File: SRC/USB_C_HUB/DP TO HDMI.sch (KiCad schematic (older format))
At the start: 35 parts, among them U6 MCDP2900, U7 ZLDO1117G12TA, Y1 27MHz

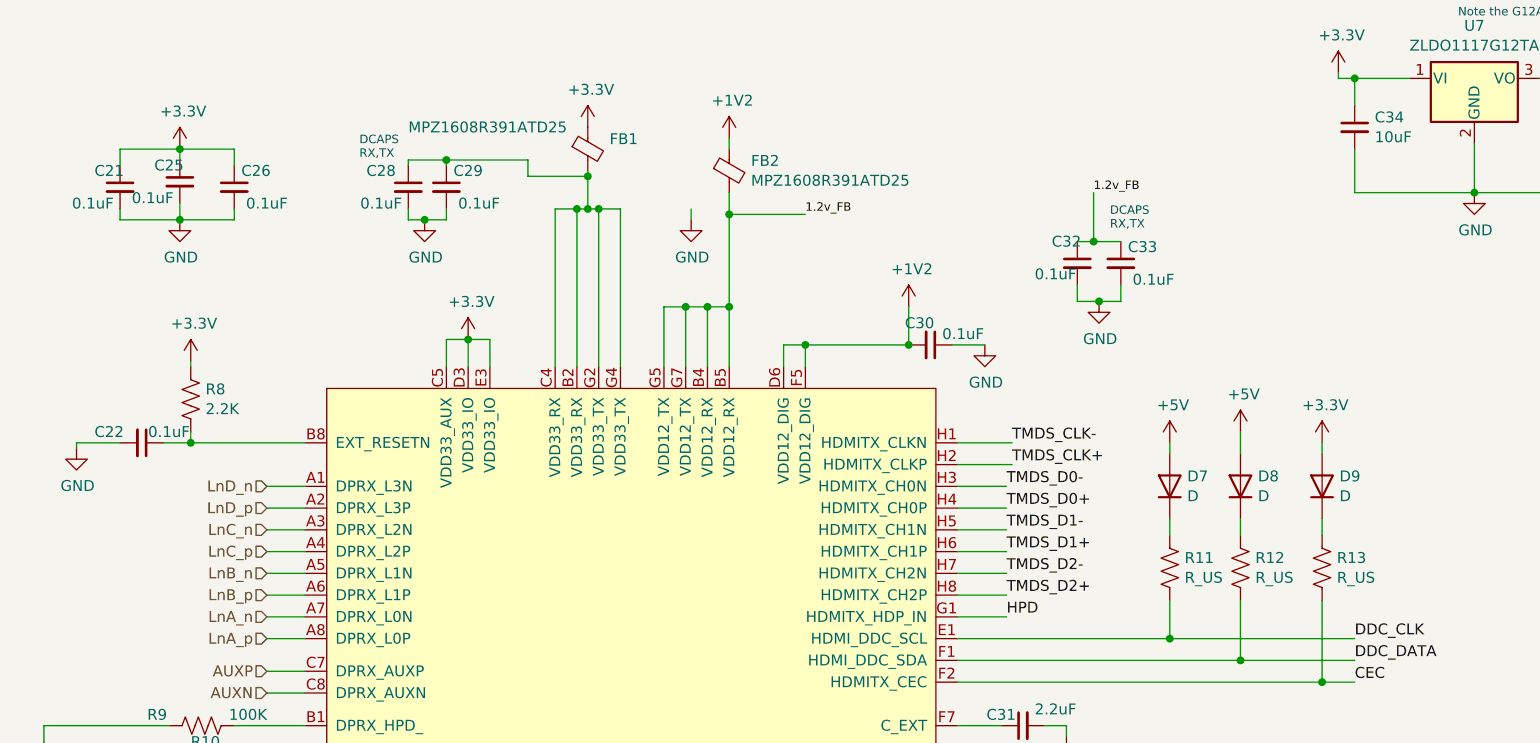
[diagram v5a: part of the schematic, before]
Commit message: schematic capture and footprint assignment complete. Pending approval
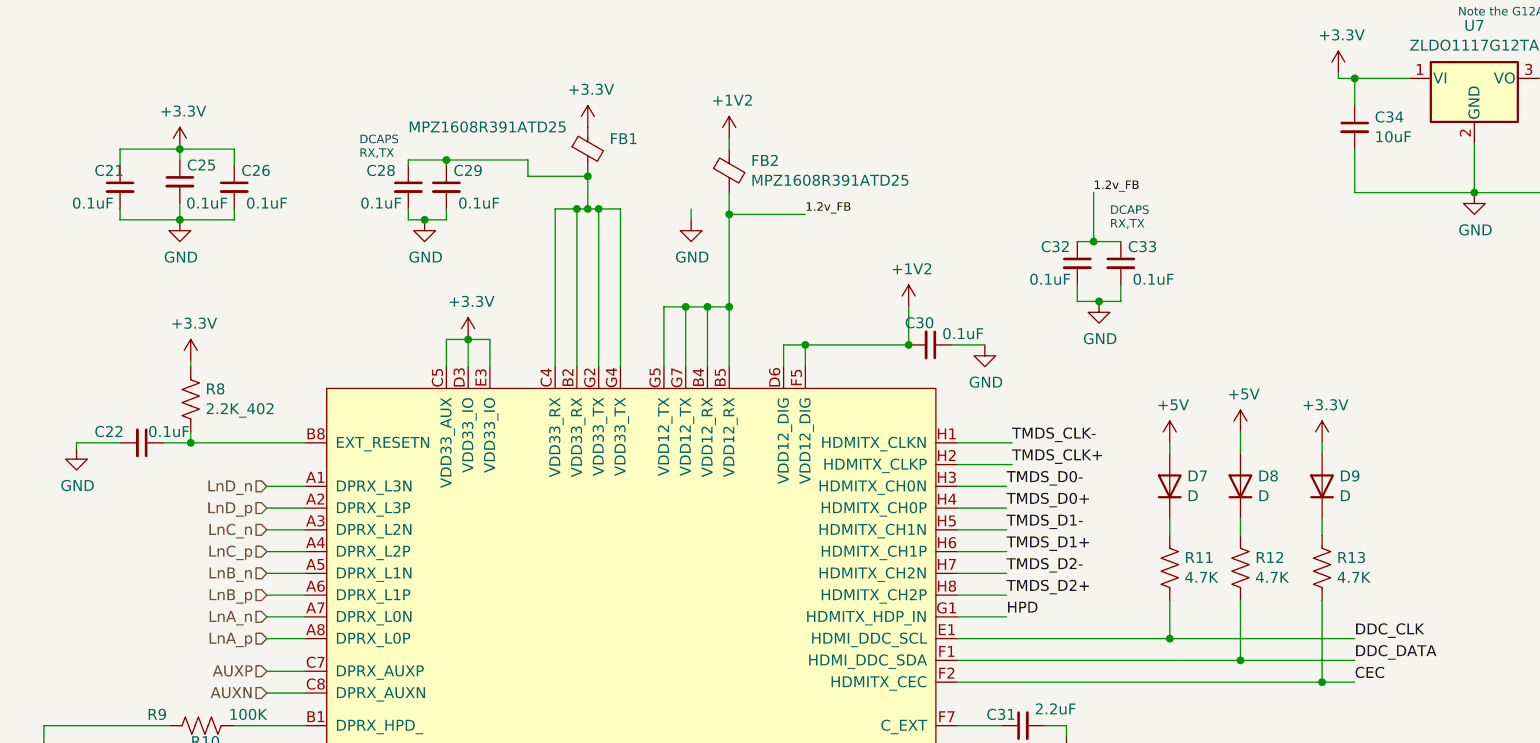
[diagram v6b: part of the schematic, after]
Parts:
- C20, C21, C22, C23, C24, C25, C26, C27, C28, C29, C30, C31, C32, C33: footprint (none) -> Capacitor_SMD:C_0402_1005Metric
- C34, C35: footprint (none) -> Capacitor_SMD:C_0603_1608Metric
- D7, D8, D9: footprint (none) -> Diode_SMD:D_SOD-323; Mfr No. (none) -> B5817WS
- FB1, FB2: footprint Resistor_SMD:R_0603_1608Metric -> Inductor_SMD:L_0603_1608Metric
- HDMI1: footprint (none) -> OLIMEX_Connectors-FP:HDMI-SWM-19
- R10: footprint (none) -> Resistor_SMD:R_0603_1608Metric; Mfr No. (none) -> ARG03BTC2490
- R11: value R_US -> 4.7K; footprint (none) -> Resistor_SMD:R_0402_1005Metric; Mfr No. (none) -> 0402WGF4701TCE
- R12, R13: value R_US -> 4.7K; footprint (none) -> Resistor_SMD:R_0402_1005Metric
- R8: value 2.2K -> 2.2K_402; footprint (none) -> Resistor_SMD:R_0402_1005Metric; Mfr No. (none) -> 0402WGJ0222TCE
- R9: footprint (none) -> Resistor_SMD:R_0805_2012Metric; Mfr No. (none) -> 0805W8F1003T5E
- U6: footprint (none) -> footprints:BGA64C100P8X8_1000X800X120N
- Y1: footprint (none) -> Crystal:Crystal_HC33-U_Horizontal_1EP_style1
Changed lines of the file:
@@
 F 0 "HDMI1" H 8431 2804 50  0000 R CNN
 F 1 "HDMI-SWM-19" H 8431 2895 50  0000 R CNN
-F 2 "" H 8605 3000 20  0001 C CNN
+F 2 "OLIMEX_Connectors-FP:HDMI-SWM-19" H 8605 3000 20  0001 C CNN
 F 3 "" H 8575 2850 60  0000 C CNN
 	1    8575 2850
@@
 P 1400 2375
 F 0 "R8" H 1468 2421 50  0000 L CNN
-F 1 "2.2K" H 1468 2330 50  0000 L CNN
-F 2 "" V 1440 2365 50  0001 C CNN
+F 1 "2.2K_402" H 1468 2330 50  0000 L CNN
+F 2 "Resistor_SMD:R_0402_1005Metric" V 1440 2365 50  0001 C CNN
 F 3 "~" H 1400 2375 50  0001 C CNN
+F 4 "0402WGJ0222TCE" H 1400 2375 50  0001 C CNN "Mfr No."
 	1    1400 2375
 	1    0    0    -1
@@
 F 0 "R10" V 1375 3975 50  0000 L CNN
 F 1 "249OHM/1%" V 1550 3800 50  0000 L CNN
-F 2 "" V 1490 4015 50  0001 C CNN
+F 2 "Resistor_SMD:R_0603_1608Metric" V 1490 4015 50  0001 C CNN
 F 3 "~" H 1450 4025 50  0001 C CNN
+F 4 "ARG03BTC2490" V 1450 4025 50  0001 C CNN "Mfr No."
 	1    1450 4025
 	0    1    1    0
@@
 F 0 "C34" H 6842 1171 50  0000 L CNN
 F 1 "10uF" H 6842 1080 50  0000 L CNN
-F 2 "" H 6750 1125 50  0001 C CNN
+F 2 "Capacitor_SMD:C_0603_1608Metric" H 6750 1125 50  0001 C CNN
 F 3 "~" H 6750 1125 50  0001 C CNN
 	1    6750 1125
@@
 F 0 "C35" H 8017 1221 50  0000 L CNN
 F 1 "10uF" H 8017 1130 50  0000 L CNN
-F 2 "" H 7925 1175 50  0001 C CNN
+F 2 "Capacitor_SMD:C_0603_1608Metric" H 7925 1175 50  0001 C CNN
 F 3 "~" H 7925 1175 50  0001 C CNN
 	1    7925 1175
@@
 F 0 "U6" H 3900 -1100 50  0000 C CNN
 F 1 "MCDP2900" H 3950 -1200 50  0000 C CNN
-F 2 "" H 5925 1475 50  0001 C CNN
+F 2 "footprints:BGA64C100P8X8_1000X800X120N" H 5925 1475 50  0001 C CNN
 F 3 "" H 5925 1475 50  0001 C CNN
 	1    3275 2325
@@
 U 1 1 61889911
 P 3225 1225
+AR Path="/64E160D5/61889911" Ref="FB1"  Part="1"
+AR Path="/6609E24E/61889911" Ref="FB1"  Part="1"
 F 0 "FB1" H 3325 1271 50  0000 L CNN
 F 1 "MPZ1608R391ATD25" H 2400 1325 50  0000 L CNN
-F 2 "Resistor_SMD:R_0603_1608Metric" V 3155 1225 50  0001 C CNN
+F 2 "Inductor_SMD:L_0603_1608Metric" V 3155 1225 50  0001 C CNN
 F 3 "~" H 3225 1225 50  0001 C CNN
 	1    3225 1225
@@
 F 0 "C29" H 2675 1475 50  0000 C CNN
 F 1 "0.1uF" H 2725 1325 50  0000 C CNN
-F 2 "" H 2575 1400 50  0001 C CNN
+F 2 "Capacitor_SMD:C_0402_1005Metric" H 2575 1400 50  0001 C CNN
 F 3 "~" H 2575 1400 50  0001 C CNN
 	1    2575 1400
@@
 F 0 "C28" H 2275 1475 50  0000 C CNN
 F 1 "0.1uF" H 2275 1325 50  0000 C CNN
-F 2 "" H 2400 1400 50  0001 C CNN
+F 2 "Capacitor_SMD:C_0402_1005Metric" H 2400 1400 50  0001 C CNN
 F 3 "~" H 2400 1400 50  0001 C CNN
 	1    2400 1400
@@
 F 0 "FB2" H 3975 1371 50  0000 L CNN
 F 1 "MPZ1608R391ATD25" H 3975 1280 50  0000 L CNN
-F 2 "Resistor_SMD:R_0603_1608Metric" V 3805 1325 50  0001 C CNN
+F 2 "Inductor_SMD:L_0603_1608Metric" V 3805 1325 50  0001 C CNN
 F 3 "~" H 3875 1325 50  0001 C CNN
 	1    3875 1325
@@
 F 0 "C20" H 950 6850 50  0000 C CNN
 F 1 "0.1uF" H 1175 6825 50  0000 C CNN
-F 2 "" H 1050 6900 50  0001 C CNN
+F 2 "Capacitor_SMD:C_0402_1005Metric" H 1050 6900 50  0001 C CNN
 F 3 "~" H 1050 6900 50  0001 C CNN
 	1    1050 6900
@@
 F 0 "Y1" V 1554 6619 50  0000 L CNN
 F 1 "27MHz" V 1645 6619 50  0000 L CNN
-F 2 "" H 1600 6375 50  0001 C CNN
+F 2 "Crystal:Crystal_HC33-U_Horizontal_1EP_style1" H 1600 6375 50  0001 C CNN
 F 3 "~" H 1600 6375 50  0001 C CNN
 F 4 "ABM8G-27.000MHZ-B4Y-T" V 1600 6375 50  0001 C CNN "Mfr No."
@@
 F 0 "C23" V 1325 6275 50  0000 C CNN
 F 1 "22pF" V 1350 6025 50  0000 C CNN
-F 2 "" H 1275 6175 50  0001 C CNN
+F 2 "Capacitor_SMD:C_0402_1005Metric" H 1275 6175 50  0001 C CNN
 F 3 "~" H 1275 6175 50  0001 C CNN
 	1    1275 6175
@@
 F 0 "C24" V 1375 6775 50  0000 C CNN
 F 1 "22pF" V 1350 6525 50  0000 C CNN
-F 2 "" H 1300 6675 50  0001 C CNN
+F 2 "Capacitor_SMD:C_0402_1005Metric" H 1300 6675 50  0001 C CNN
 F 3 "~" H 1300 6675 50  0001 C CNN
 	1    1300 6675
@@
 F 0 "C31" V 5275 3975 50  0000 C CNN
 F 1 "2.2uF" V 5300 3725 50  0000 C CNN
-F 2 "" H 5225 3875 50  0001 C CNN
+F 2 "Capacitor_SMD:C_0402_1005Metric" H 5225 3875 50  0001 C CNN
 F 3 "~" H 5225 3875 50  0001 C CNN
 	1    5225 3875
@@
 F 0 "C27" H 1600 5100 50  0000 C CNN
 F 1 "0.1uf" H 1575 5250 50  0000 C CNN
-F 2 "" H 1700 5175 50  0001 C CNN
+F 2 "Capacitor_SMD:C_0402_1005Metric" H 1700 5175 50  0001 C CNN
 F 3 "~" H 1700 5175 50  0001 C CNN
 	1    1700 5175
@@
 F 0 "C30" V 4700 2075 50  0000 C CNN
 F 1 "0.1uF" V 4750 2275 50  0000 C CNN
-F 2 "" H 4800 2125 50  0001 C CNN
+F 2 "Capacitor_SMD:C_0402_1005Metric" H 4800 2125 50  0001 C CNN
 F 3 "~" H 4800 2125 50  0001 C CNN
 	1    4800 2125
@@
 U 1 1 61AF13C1
 P 5475 1750
-F 0 "C32" H 5425 1850 50  0000 C CNN
-F 1 "0.1uF" H 5375 1700 50  0000 C CNN
-F 2 "" H 5475 1750 50  0001 C CNN
+F 0 "C32" H 5375 1825 50  0000 C CNN
+F 1 "0.1uF" H 5350 1675 50  0000 C CNN
+F 2 "Capacitor_SMD:C_0402_1005Metric" H 5475 1750 50  0001 C CNN
 F 3 "~" H 5475 1750 50  0001 C CNN
 	1    5475 1750
@@
 F 0 "C33" H 5775 1825 50  0000 C CNN
 F 1 "0.1uF" H 5825 1675 50  0000 C CNN
-F 2 "" H 5675 1750 50  0001 C CNN
+F 2 "Capacitor_SMD:C_0402_1005Metric" H 5675 1750 50  0001 C CNN
 F 3 "~" H 5675 1750 50  0001 C CNN
 	1    5675 1750
@@
 F 0 "C26" H 1700 1475 50  0000 C CNN
 F 1 "0.1uF" H 1750 1325 50  0000 C CNN
-F 2 "" H 1600 1400 50  0001 C CNN
+F 2 "Capacitor_SMD:C_0402_1005Metric" H 1600 1400 50  0001 C CNN
 F 3 "~" H 1600 1400 50  0001 C CNN
 	1    1600 1400
@@
 U 1 1 61B8F7AE
 P 1350 1375
-F 0 "C25" H 1300 1450 50  0000 C CNN
-F 1 "0.1uF" H 1225 1300 50  0000 C CNN
-F 2 "" H 1350 1375 50  0001 C CNN
+F 0 "C25" H 1450 1450 50  0000 C CNN
+F 1 "0.1uF" H 1475 1275 50  0000 C CNN
+F 2 "Capacitor_SMD:C_0402_1005Metric" H 1350 1375 50  0001 C CNN
 F 3 "~" H 1350 1375 50  0001 C CNN
 	1    1350 1375
@@
 F 0 "C21" H 1025 1475 50  0000 C CNN
 F 1 "0.1uF" H 950 1325 50  0000 C CNN
-F 2 "" H 1075 1400 50  0001 C CNN
+F 2 "Capacitor_SMD:C_0402_1005Metric" H 1075 1400 50  0001 C CNN
 F 3 "~" H 1075 1400 50  0001 C CNN
 	1    1075 1400
@@
 P 5900 3150
 F 0 "R11" H 5968 3196 50  0000 L CNN
-F 1 "R_US" H 5968 3105 50  0000 L CNN
-F 2 "" V 5940 3140 50  0001 C CNN
+F 1 "4.7K" H 5968 3105 50  0000 L CNN
+F 2 "Resistor_SMD:R_0402_1005Metric" V 5940 3140 50  0001 C CNN
 F 3 "~" H 5900 3150 50  0001 C CNN
+F 4 "0402WGF4701TCE" H 5900 3150 50  0001 C CNN "Mfr No."
 	1    5900 3150
 	1    0    0    -1
@@
 F 0 "D7" V 5946 2695 50  0000 R CNN
 F 1 "D" V 5855 2695 50  0000 R CNN
-F 2 "" H 5900 2775 50  0001 C CNN
+F 2 "Diode_SMD:D_SOD-323" H 5900 2775 50  0001 C CNN
 F 3 "~" H 5900 2775 50  0001 C CNN
+F 4 "B5817WS" V 5900 2775 50  0001 C CNN "Mfr No."
 	1    5900 2775
 	0    -1   -1   0
@@
 P 6225 3150
 F 0 "R12" H 6293 3196 50  0000 L CNN
-F 1 "R_US" H 6293 3105 50  0000 L CNN
-F 2 "" V 6265 3140 50  0001 C CNN
+F 1 "4.7K" H 6293 3105 50  0000 L CNN
+F 2 "Resistor_SMD:R_0402_1005Metric" V 6265 3140 50  0001 C CNN
 F 3 "~" H 6225 3150 50  0001 C CNN
 	1    6225 3150
@@
 F 0 "D8" V 6271 2695 50  0000 R CNN
 F 1 "D" V 6180 2695 50  0000 R CNN
-F 2 "" H 6225 2775 50  0001 C CNN
+F 2 "Diode_SMD:D_SOD-323" H 6225 2775 50  0001 C CNN
 F 3 "~" H 6225 2775 50  0001 C CNN
+F 4 "B5817WS" V 6225 2775 50  0001 C CNN "Mfr No."
 	1    6225 2775
 	0    -1   -1   0
@@
 P 6600 3150
 F 0 "R13" H 6668 3196 50  0000 L CNN
-F 1 "R_US" H 6668 3105 50  0000 L CNN
-F 2 "" V 6640 3140 50  0001 C CNN
+F 1 "4.7K" H 6668 3105 50  0000 L CNN
+F 2 "Resistor_SMD:R_0402_1005Metric" V 6640 3140 50  0001 C CNN
 F 3 "~" H 6600 3150 50  0001 C CNN
 	1    6600 3150
@@
 F 0 "D9" V 6646 2695 50  0000 R CNN
 F 1 "D" V 6555 2695 50  0000 R CNN
-F 2 "" H 6600 2775 50  0001 C CNN
+F 2 "Diode_SMD:D_SOD-323" H 6600 2775 50  0001 C CNN
 F 3 "~" H 6600 2775 50  0001 C CNN
+F 4 "B5817WS" V 6600 2775 50  0001 C CNN "Mfr No."
 	1    6600 2775
 	0    -1   -1   0
@@
 F 0 "R9" V 1400 3625 50  0000 L CNN
 F 1 "100K" V 1400 4000 50  0000 L CNN
-F 2 "" V 1490 3865 50  0001 C CNN
+F 2 "Resistor_SMD:R_0805_2012Metric" V 1490 3865 50  0001 C CNN
 F 3 "~" H 1450 3875 50  0001 C CNN
+F 4 "0805W8F1003T5E" V 1450 3875 50  0001 C CNN "Mfr No."
 	1    1450 3875
 	0    1    1    0
@@
 F 0 "C22" V 1125 2425 50  0000 C CNN
 F 1 "0.1uF" V 1125 2700 50  0000 C CNN
-F 2 "" H 1175 2575 50  0001 C CNN
+F 2 "Capacitor_SMD:C_0402_1005Metric" H 1175 2575 50  0001 C CNN
 F 3 "~" H 1175 2575 50  0001 C CNN
 	1    1175 2575

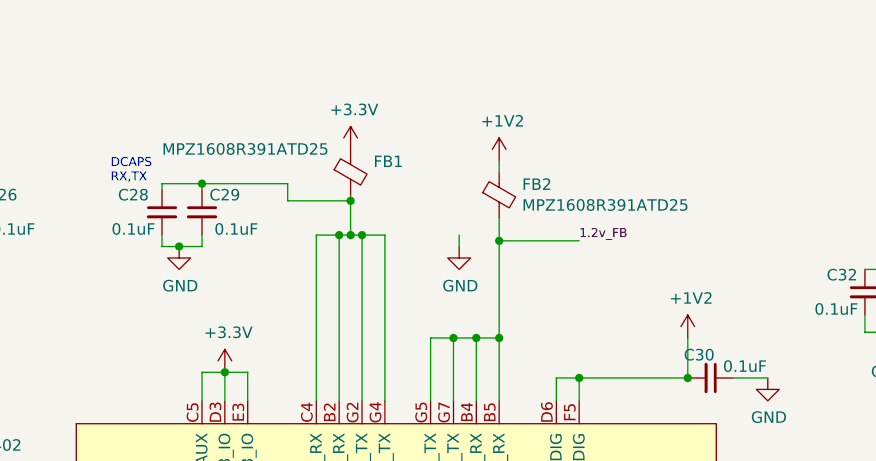
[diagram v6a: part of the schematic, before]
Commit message: updated BOM, minor change in schematic
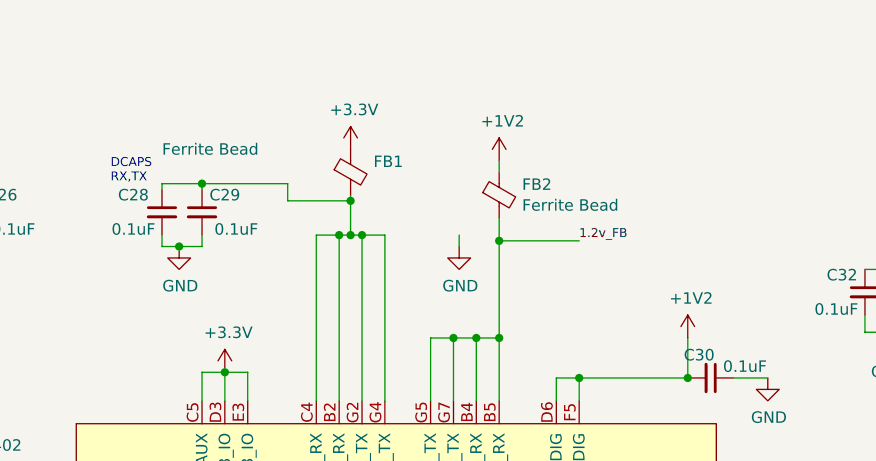
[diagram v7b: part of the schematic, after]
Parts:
- FB1, FB2: value MPZ1608R391ATD25 -> Ferrite Bead
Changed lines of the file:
@@
 AR Path="/6609E24E/61889911" Ref="FB1"  Part="1"
 F 0 "FB1" H 3325 1271 50  0000 L CNN
-F 1 "MPZ1608R391ATD25" H 2400 1325 50  0000 L CNN
+F 1 "Ferrite Bead" H 2400 1325 50  0000 L CNN
 F 2 "Inductor_SMD:L_0603_1608Metric" V 3155 1225 50  0001 C CNN
 F 3 "~" H 3225 1225 50  0001 C CNN
@@
 P 3875 1325
 F 0 "FB2" H 3975 1371 50  0000 L CNN
-F 1 "MPZ1608R391ATD25" H 3975 1280 50  0000 L CNN
+F 1 "Ferrite Bead" H 3975 1280 50  0000 L CNN
 F 2 "Inductor_SMD:L_0603_1608Metric" V 3805 1325 50  0001 C CNN
 F 3 "~" H 3875 1325 50  0001 C CNN
